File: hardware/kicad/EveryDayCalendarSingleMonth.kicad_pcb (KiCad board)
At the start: 2 copper layers, 100 x 100 mm, 154 parts, among them J1 Conn_01x03, J2 Conn_01x02, J3 Conn_01x06, Q1 PN2222A, Q2 PN2222A, U1 ESP32-WROOM-32E, U2 74AHC1G125, U3 LT1117-3.3

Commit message: First step in PCB layout, getting everything sorted into their general locations
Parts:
- removed the C26 at (125.9, -86.6)
- removed C51, C52, C53, C54, C55, C56: 1uF,25V,X5R, tom-passives:C_0402_1005Metric
- removed TP13, TP14, TP3, TP4: TestPoint, TestPoint:TestPoint_Pad_2.5x2.5mm
- D19: value LED -> STATUS_LED
- moved SW_RESET1 259.5 mm to (27.0, 135.5)
- moved TP_BOTTOM_GND1 250.4 mm to (70.0, 152.0)
- moved C11 248.8 mm to (127.0, 132.5), turned to 180 degrees
- moved C10 243.6 mm to (127.5, 136.5), turned to 180 degrees
- moved C50 238.8 mm to (59.0, 114.5), turned to 90 degrees
- moved C2 235.8 mm to (127.0, 129.5), turned to 180 degrees
- moved SW_WIN1 234.5 mm to (123.0, 118.0)
- moved J3_PROGRAMING_PIN1 233.1 mm to (54.0, 114.0)
- moved J1_ONE_WIRE1 231.4 mm to (147.0, 120.5), turned to 180 degrees
- moved R3 229.4 mm to (144.0, 118.0), turned to 180 degrees
- moved D30 225.7 mm to (70.0, 95.0)
- moved R4 225.4 mm to (65.0, 125.5), turned to -90 degrees
- moved SW_RESET_PROGRAMING1 223.6 mm to (27.0, 124.5)
- moved C25 223.1 mm to (96.0, 105.0), turned to -90 degrees
- moved SW_WEEK5 221.6 mm to (56.8, 95.0)
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- renumbered C18 to C11, C19 to C12, C20 to C13, C21 to C14, C22 to C15, C23 to C16, C24 to C17, C25 to C18, C27 to C20, C28 to C21, C29 to C22, C30 to C23, C31 to C24, C32 to C25, C33 to C26, C34 to C27, C35 to C28, C36 to C29, C11 to C3, C37 to C30, C38 to C31, C39 to C32, C40 to C33, C41 to C34, C42 to C35, C43 to C36, C44 to C37, C45 to C38, C46 to C39, C12 to C4, C47 to C40, C48 to C41, C49 to C42, C50 to C43, C13 to C5, C57 to C50, C14 to C6, C15 to C7, C16 to C8, C17 to C9, C4 to C_ROW1, C5 to C_ROW2, C6 to C_ROW3, C7 to C_ROW4, C8 to C_ROW5, C9 to C_ROW6, C3 to C_ROW_STATUS1, J1 to J1_ONE_WIRE1, J2 to J2_POWER_IN1, J3 to J3_PROGRAMING_PIN1, Q1 to Q1_PROGRAMING1, Q2 to Q2_PROGRAMING1, SW_RESET2 to SW_RESET1, SW_RESET1 to SW_RESET_PROGRAMING1, TP2 to TP1, TP1 to TP1_IO1, TP11 to TP_BOTTOM_5V1, TP9 to TP_BOTTOM_GND1, TP15 to TP_CORNER_1, TP16 to TP_CORNER_2, TP17 to TP_CORNER_3, TP18 to TP_CORNER_4, TP8 to TP_LEFT_5V1, TP6 to TP_LEFT_GND1, TP12 to TP_RIGHT_5V1, TP10 to TP_RIGHT_GND1, TP7 to TP_TOP_5V1, TP5 to TP_TOP_GND1, U2 to U1, U1 to U_CPU1, U3 to U_POWER1
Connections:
- SW_RESET1 pad 1: /RESET -> unconnected-(SW_RESET1-Pad1)

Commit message: Working on getting all the traces done
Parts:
- removed C12, C3: 1uF,25V,X5R, tom-passives:C_0402_1005Metric
- removed TP1_IO1: TestPoint, TestPoint:TestPoint_Pad_D2.0mm
- added SW_WIN2: Switch_SW_Push, calendar:SW_Push_1P1T_NO_6x6mm_H9.5mm, F.Cu at (145.5, 65.0)
- added TP_LEDLINK_IN1: TestPoint, TestPoint:TestPoint_Pad_2.5x2.5mm, F.Cu at (160.0, 110.5)
- moved C1 100.4 mm to (69.7, 120.5)
- moved J1_ONE_WIRE1 94.0 mm to (53.0, 120.5)
- moved U1 90.4 mm to (117.0, 117.0)
- moved R3 88.5 mm to (55.5, 118.5), turned to -90 degrees
- moved DAY6 76.6 mm to (67.0, 105.0), turned to 180 degrees
- moved DAY37 72.1 mm to (133.0, 55.0), turned to 180 degrees
- moved SW_WIN1 66.9 mm to (145.5, 55.0), turned to 90 degrees
- moved DAY5 61.7 mm to (67.0, 95.0), turned to 180 degrees
- moved DAY7 58.0 mm to (78.0, 55.0), turned to 180 degrees
- moved DAY38 57.3 mm to (133.0, 65.0), turned to 180 degrees
- moved D1 56.4 mm to (70.2, 126.0)
- moved SW_CAL_PREV1 55.4 mm to (145.5, 85.0), turned to 90 degrees
- moved DAY12 53.8 mm to (78.0, 105.0), turned to 180 degrees
- moved R2 52.1 mm to (71.7, 126.0)
- moved DAY36 52.0 mm to (122.0, 105.0), turned to 180 degrees
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- renumbered C20 to C19, C21 to C20, C22 to C21, C23 to C22, C24 to C23, C25 to C24, C26 to C25, C27 to C26, C28 to C27, C29 to C28, C30 to C29, C31 to C30, C32 to C31, C33 to C32, C34 to C33, C35 to C34, C36 to C35, C37 to C36, C38 to C37, C39 to C38, C40 to C39, C41 to C40, C42 to C41, C43 to C42, C50 to C43, D19 to D1, D1 to DAY1, D10 to DAY10, D11 to DAY11, D12 to DAY12, D13 to DAY13, D14 to DAY14, D15 to DAY15, D16 to DAY16, D17 to DAY17, D18 to DAY18, D20 to DAY19, D2 to DAY2, D21 to DAY20, D22 to DAY21, D23 to DAY22, D24 to DAY23, D25 to DAY24, D26 to DAY25, D27 to DAY26, D28 to DAY27, D29 to DAY28, D30 to DAY29, D3 to DAY3, D31 to DAY30, D32 to DAY31, D33 to DAY32, D34 to DAY33, D35 to DAY34, D36 to DAY35, D37 to DAY36, D38 to DAY37, D39 to DAY38, D40 to DAY39, D4 to DAY4, D41 to DAY40, D42 to DAY41, D43 to DAY42, D5 to DAY5, D6 to DAY6, D7 to DAY7, D8 to DAY8, D9 to DAY9, TP_CORNER_3 to TP_CORNER_2, TP_CORNER_4 to TP_CORNER_3, TP_CORNER_2 to TP_CORNER_4, TP1 to TP_LEDLINK_OUT1
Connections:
- net /BUTTON_WIN renamed /BUTTON_WIN1
- net /LED_LINK renamed Net-(R1-Pad2)
- DAY1 pad 3: Net-(D1-Pad3) -> Net-(U1-Pad4)
- DAY42 pad 1: Net-(D43-Pad1) -> Net-(DAY42-Pad1)
- D_S1 pad 3: Net-(D_S1-Pad3) -> Net-(DAY42-Pad1)
- D_S3 pad 1: Net-(D1-Pad3) -> Net-(D_S3-Pad1)
- TP_LEDLINK_OUT1 pad 1: Net-(D43-Pad1) -> Net-(D_S3-Pad1)
- U1 pad 4: Net-(D_S1-Pad3) -> Net-(U1-Pad4)
- U_CPU1 pad 10: /WEEK5 -> /DAY6
- U_CPU1 pad 11: /WEEK6 -> /DAY7
- U_CPU1 pad 13: /DAY3 -> /DAY1
- U_CPU1 pad 14: /DAY2 -> /PIN_LED_CAL
- U_CPU1 pad 23: /DAY4 -> /DAY2
- U_CPU1 pad 26: /PIN_TEST_POINT -> /WEEK1
- U_CPU1 pad 27: /DAY5 -> /WEEK2
- U_CPU1 pad 28: /DAY6 -> /WEEK3
- U_CPU1 pad 29: /DAY1 -> /WEEK4
- U_CPU1 pad 30: /DAY7 -> /WEEK6
- U_CPU1 pad 31: /WEEK1 -> /WEEK5
- U_CPU1 pad 33: /WEEK2 -> /DAY3
- U_CPU1 pad 36: /WEEK3 -> /DAY4
- U_CPU1 pad 37: /WEEK4 -> /DAY5
- U_CPU1 pad 9: /PIN_LED_CAL -> /BUTTON_WIN2
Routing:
- net +5V: track 0.00 -> 680.1 mm
- net /DAY3: track 0.00 -> 146.3 mm
- net /DAY2: track 0.00 -> 143.9 mm
- net /DAY4: track 0.00 -> 93.4 mm
- net /WEEK1: track 0.00 -> 93.1 mm
- net Net-(DAY40-Pad1): track 0.00 -> 86.3 mm
- net Net-(DAY41-Pad1): track 0.00 -> 85.9 mm
- net Net-(DAY38-Pad1): track 0.00 -> 85.7 mm
- net Net-(DAY2-Pad3): track 0.00 -> 85.4 mm
- net Net-(DAY4-Pad3): track 0.00 -> 85.1 mm
- net /WEEK2: track 0.00 -> 84.0 mm
- net /DAY5: track 0.00 -> 83.6 mm
- net /WEEK3: track 0.00 -> 75.2 mm
- net /DAY6: track 0.00 -> 73.2 mm
- net /WEEK5: track 0.00 -> 70.2 mm
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
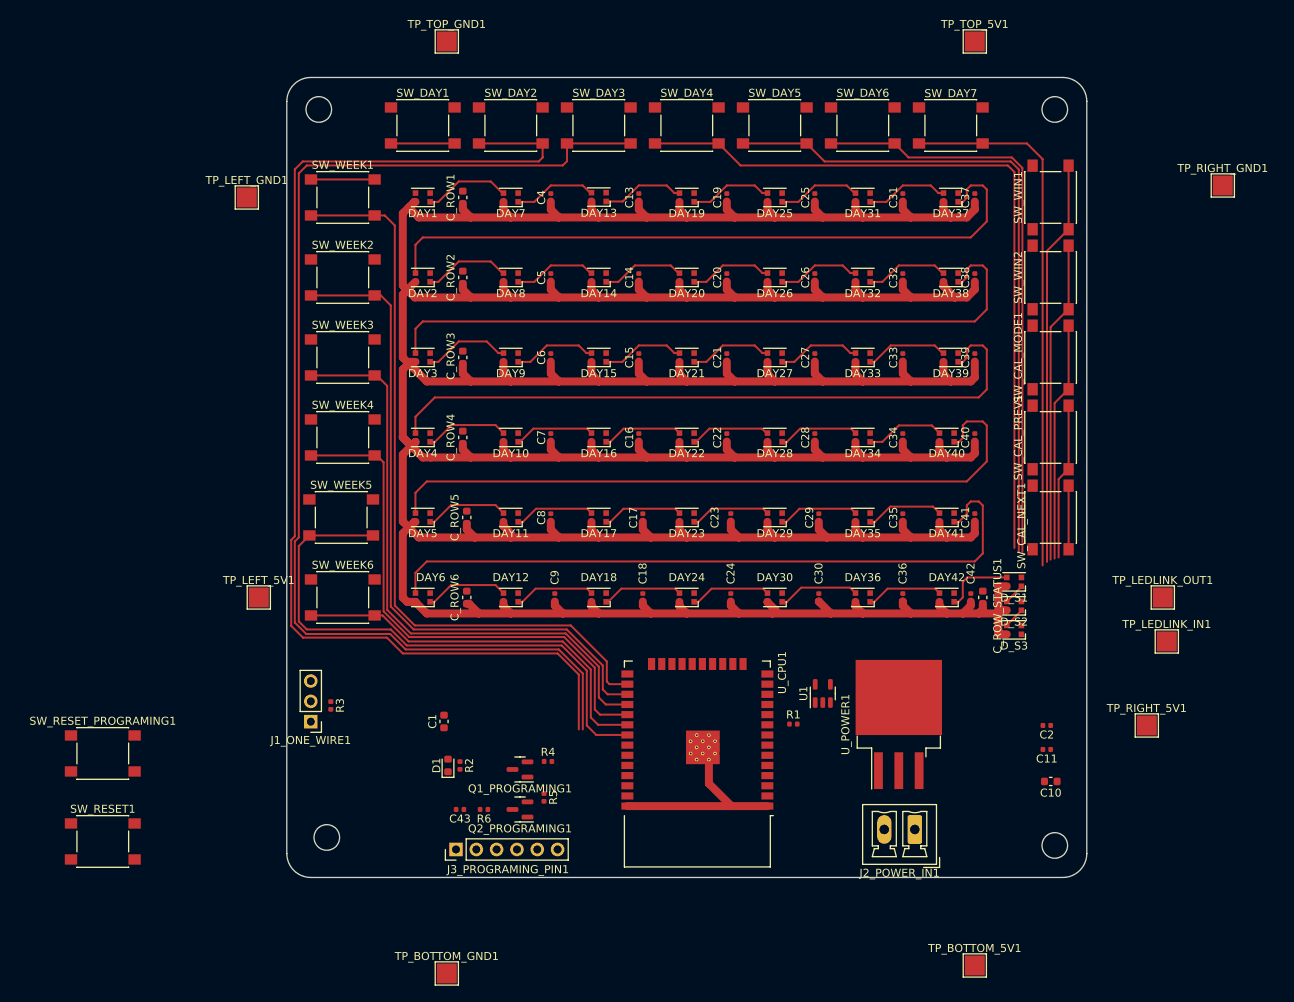
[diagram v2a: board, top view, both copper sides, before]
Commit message: added GND base
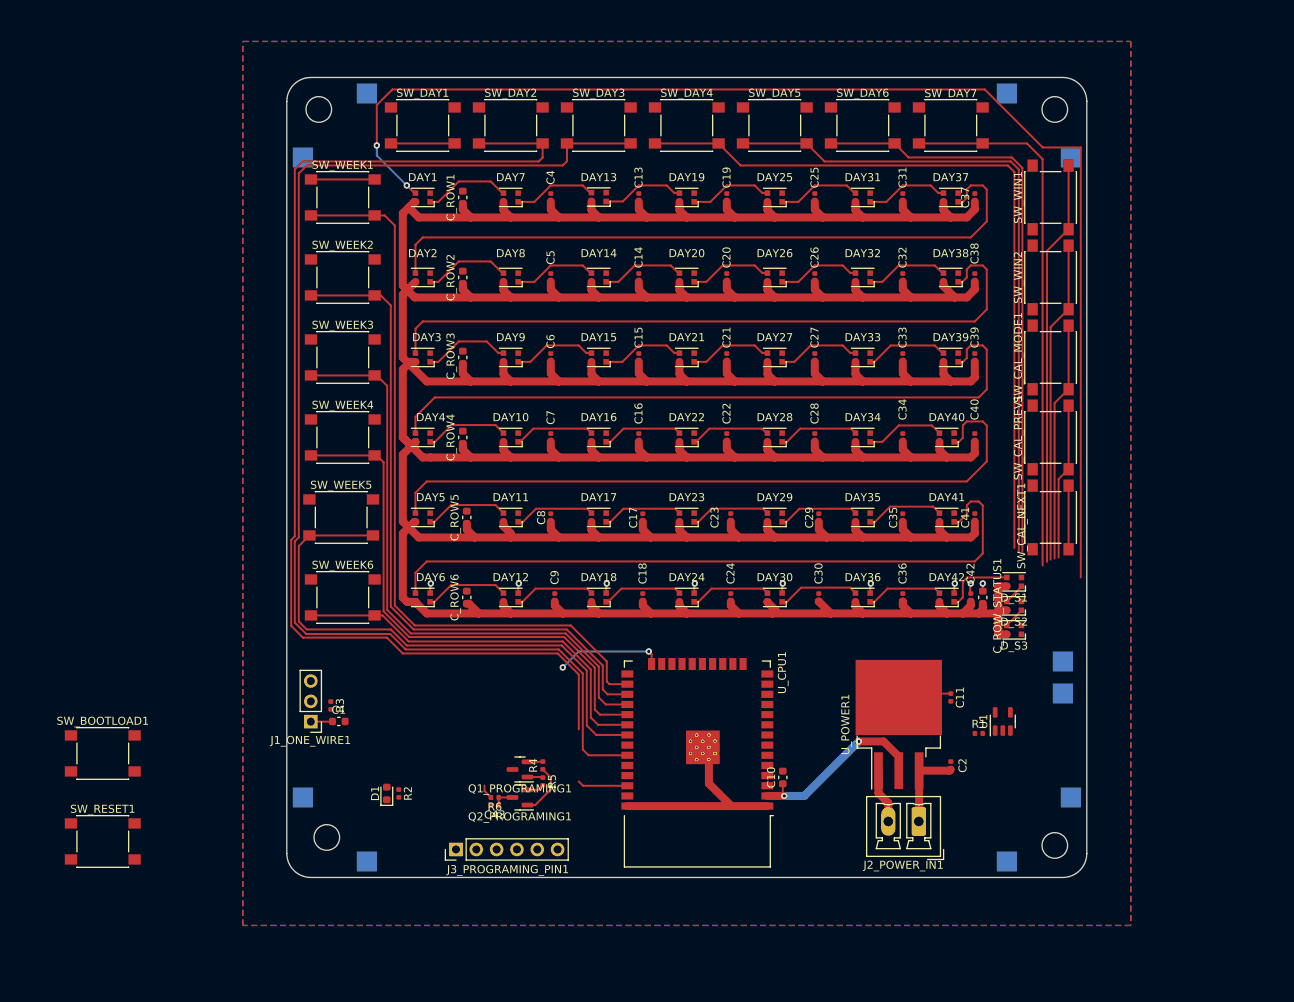
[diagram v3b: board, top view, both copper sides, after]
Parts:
- TP_BOTTOM_5V1, TP_BOTTOM_GND1, TP_LEDLINK_IN1, TP_LEDLINK_OUT1, TP_LEFT_5V1, TP_LEFT_GND1, TP_RIGHT_5V1, TP_RIGHT_GND1, TP_TOP_5V1, TP_TOP_GND1: moved to B.Cu
- moved C10 33.5 mm to (112.0, 127.5), turned to 90 degrees
- moved TP_LEFT_5V1 25.6 mm to (52.0, 130.0), turned to 180 degrees
- moved R1 23.2 mm to (136.5, 122.0)
- moved U1 22.8 mm to (139.5, 120.5)
- moved TP_RIGHT_GND1 19.3 mm to (148.0, 50.0), turned to 180 degrees
- moved TP_BOTTOM_GND1 17.2 mm to (60.0, 138.0), turned to 180 degrees
- moved TP_LEDLINK_OUT1 14.8 mm to (147.0, 113.0), turned to 180 degrees
- moved TP_LEDLINK_IN1 14.5 mm to (147.0, 117.0), turned to 180 degrees
- moved C11 13.6 mm to (133.0, 117.5), turned to -90 degrees
- moved TP_BOTTOM_5V1 13.6 mm to (140.0, 138.0), turned to 180 degrees
- moved C1 13.2 mm to (56.5, 120.5), turned to 0 degrees
- moved TP_RIGHT_5V1 13.1 mm to (148.0, 130.0), turned to 180 degrees
- moved C2 13.0 mm to (133.0, 126.0), turned to 90 degrees
- moved TP_TOP_GND1 11.9 mm to (60.0, 42.0), turned to 180 degrees
- moved TP_LEFT_GND1 8.60 mm to (52.0, 50.0), turned to 180 degrees
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- renumbered SW_RESET_PROGRAMING1 to SW_BOOTLOAD1
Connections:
- SW_RESET1 pad 1: unconnected-(SW_RESET1-Pad1) -> /RESET
- U1 pad 5: VCC -> +5V
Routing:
- net Net-(DAY1-Pad3): track 0.00 -> 158.6 mm, vias 0 -> 2
- net +3.3V: track 0.00 -> 34.6 mm, vias 0 -> 2
- net GND: track 32.4 -> 50.4 mm, vias 0 -> 9
- net /PIN_ONE_WIRE: track 0.00 -> 13.3 mm, vias 0 -> 2
- net +5V: track 680.1 -> 691.5 mm
- net /DAY3: track 146.3 -> 154.7 mm
- net /RTS: track 0.00 -> 6.65 mm
- net /DAY4: track 93.4 -> 99.7 mm
- net /RESET: track 0.00 -> 2.73 mm
- net Net-(Q2_PROGRAMING1-Pad2): track 0.00 -> 2.15 mm
- net /DTR: track 0.00 -> 1.94 mm
- net Net-(Q1_PROGRAMING1-Pad2): track 0.00 -> 1.93 mm
- added copper zone on B.Cu, net GND
- added copper zone on F.Cu, net GND

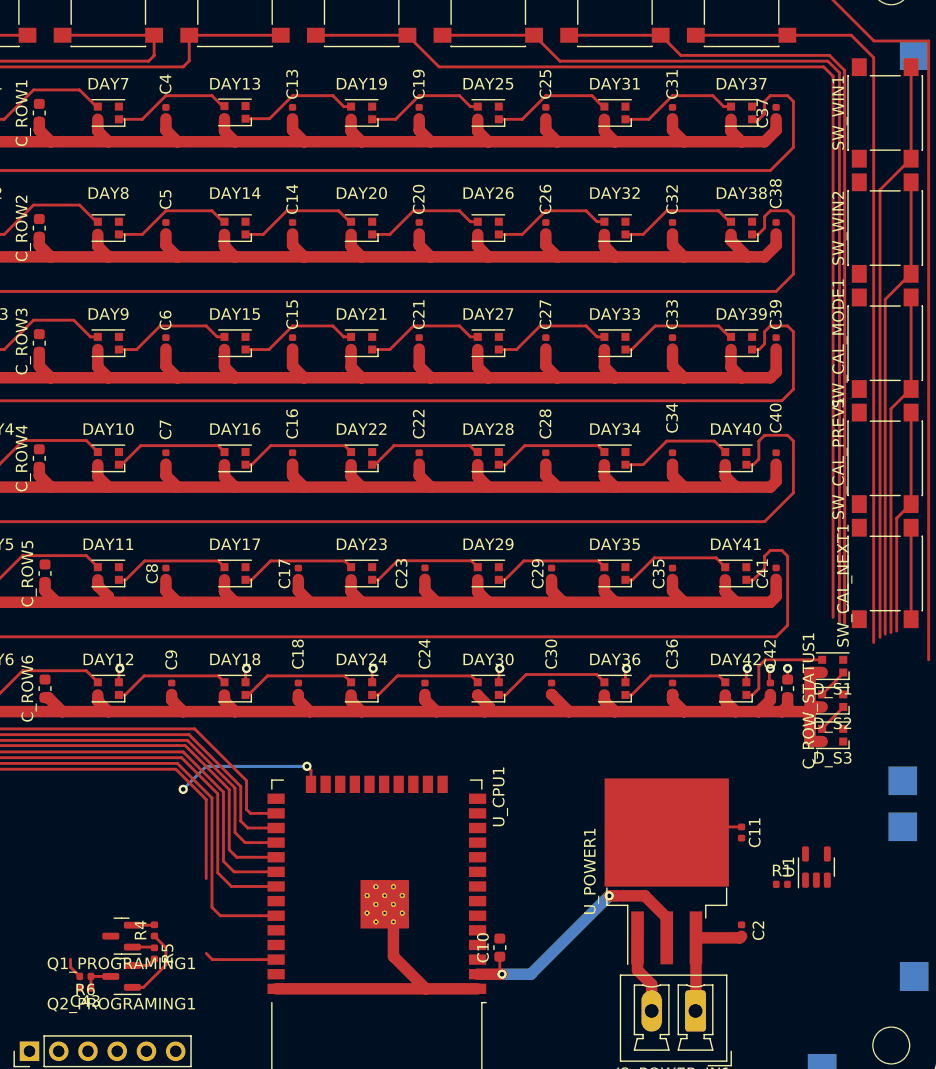
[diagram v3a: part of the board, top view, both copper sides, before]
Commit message: Added 3d part for pushbuttons
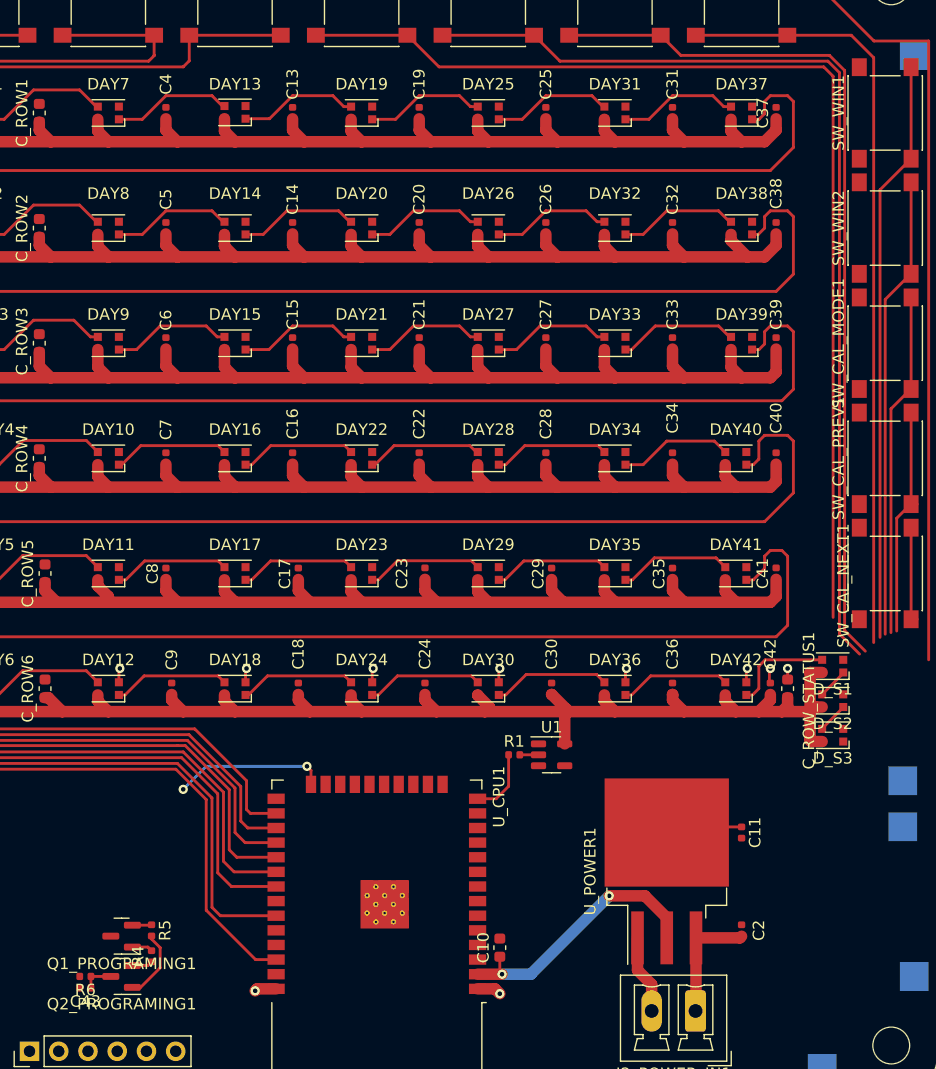
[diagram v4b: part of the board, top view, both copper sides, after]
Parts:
- moved R1 25.8 mm to (113.2, 110.8)
- moved U1 25.0 mm to (116.5, 110.8), turned to 0 degrees
- moved R4 2.26 mm to (81.8, 128.2)
- moved R5 2.02 mm to (81.8, 126.0)
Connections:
- Q1_PROGRAMING1 pad 1: /DTR -> Net-(Q1_PROGRAMING1-Pad1)
- Q1_PROGRAMING1 pad 2: Net-(Q1_PROGRAMING1-Pad2) -> /DTR
- Q2_PROGRAMING1 pad 1: /RTS -> Net-(Q2_PROGRAMING1-Pad1)
- Q2_PROGRAMING1 pad 2: Net-(Q2_PROGRAMING1-Pad2) -> /RTS
- R4 pad 2: Net-(Q1_PROGRAMING1-Pad2) -> Net-(Q1_PROGRAMING1-Pad1)
- R5 pad 2: Net-(Q2_PROGRAMING1-Pad2) -> Net-(Q2_PROGRAMING1-Pad1)
- U_CPU1 pad 23: /DAY2 -> /DAY4
- U_CPU1 pad 36: /DAY4 -> /DAY2
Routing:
- net GND: track 50.4 -> 29.9 mm, vias 9 -> 11
- net /DAY2: track 143.9 -> 154.5 mm
- net /DAY4: track 99.7 -> 93.4 mm
- net Net-(Q2_PROGRAMING1-Pad1): track 0.00 -> 6.19 mm
- net /PIN_LED_CAL: track 0.00 -> 5.88 mm
- net /RTS: track 6.65 -> 1.79 mm
- net /DAY5: track 83.6 -> 87.0 mm
- net /DAY6: track 73.2 -> 76.4 mm
- net +5V: track 691.5 -> 694.6 mm
- net Net-(Q2_PROGRAMING1-Pad2): track 2.15 -> 0.00 mm
- net Net-(Q1_PROGRAMING1-Pad2): track 1.93 -> 0.00 mm
- net +3.3V: track 34.6 -> 32.8 mm
- net Net-(Q1_PROGRAMING1-Pad1): track 0.00 -> 1.79 mm
- net Net-(R1-Pad2): track 0.00 -> 1.63 mm

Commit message: Zero errors or warnings.
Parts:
- SW_BOOTLOAD1, SW_RESET1: moved to B.Cu
- moved D1 43.4 mm to (101.2, 110.0)
- moved R2 43.4 mm to (102.8, 110.0)
- moved SW_RESET1 39.1 mm to (65.5, 128.5), turned to 180 degrees
- moved SW_BOOTLOAD1 38.7 mm to (65.5, 120.5), turned to 180 degrees
- moved R1 32.1 mm to (142.8, 123.5), turned to 90 degrees
- moved U1 27.9 mm to (142.8, 120.2), turned to 90 degrees
- moved C1 1.68 mm to (55.8, 122.0)
- moved J1_ONE_WIRE1 1.68 mm to (52.2, 122.0)
- moved R3 1.68 mm to (54.8, 120.0)
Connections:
- C1 pad 1: +3.3V -> +5V
- J1_ONE_WIRE1 pad 1: +3.3V -> +5V
- U_CPU1 pad 10: /DAY6 -> /PIN_LED_CAL
- U_CPU1 pad 11: /DAY7 -> /BUTTON_WIN1
- U_CPU1 pad 12: /BUTTON_CAL_PREV -> /DAY7
- U_CPU1 pad 13: /DAY1 -> /DAY6
- U_CPU1 pad 14: /PIN_LED_CAL -> /DAY5
- U_CPU1 pad 37: /DAY5 -> /DAY1
- U_CPU1 pad 6: /BUTTON_MODE -> /BUTTON_CAL_NEXT
- U_CPU1 pad 7: /BUTTON_WIN1 -> /BUTTON_CAL_PREV
- U_CPU1 pad 8: /BUTTON_CAL_NEXT -> /BUTTON_MODE
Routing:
- net GND: track 29.9 -> 187.2 mm, vias 11 -> 137
- net +5V: track 694.6 -> 828.9 mm, vias 0 -> 7
- net /DAY1: track 7.95 -> 135.3 mm, vias 0 -> 4
- net /BUTTON_CAL_NEXT: track 8.49 -> 88.2 mm
- net /BUTTON_CAL_PREV: track 20.0 -> 98.5 mm
- net /BUTTON_MODE: track 29.9 -> 108.2 mm
- net /BUTTON_WIN2: track 40.2 -> 118.4 mm
- net /DAY4: track 93.4 -> 153.3 mm, vias 0 -> 2
- net /RESET: track 2.73 -> 58.1 mm, vias 0 -> 3
- net +3.3V: track 32.8 -> 87.4 mm, vias 2 -> 6
- net /BUTTON_WIN1: track 51.0 -> 102.1 mm
- net /DAY7: track 67.1 -> 115.0 mm
- net /PIN_LED_CAL: track 5.88 -> 52.9 mm
- net /GPIO0: track 0.00 -> 46.0 mm, vias 0 -> 3
- net /DAY6: track 76.4 -> 121.9 mm
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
